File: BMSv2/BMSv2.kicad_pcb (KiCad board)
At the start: 2 copper layers, 44 x 41.2 mm, 126 parts, among them J1 Conn_01x05, J2 Conn_01x04_Socket, J3 Conn_01x02_Pin, J4 Conn_01x02_Pin, J5 Conn_01x03_Pin, Q1 AO3401A, Q10 MMBT3904, Q11 MMBT3904, Q12 MMBT3904, Q13 MMBT3904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

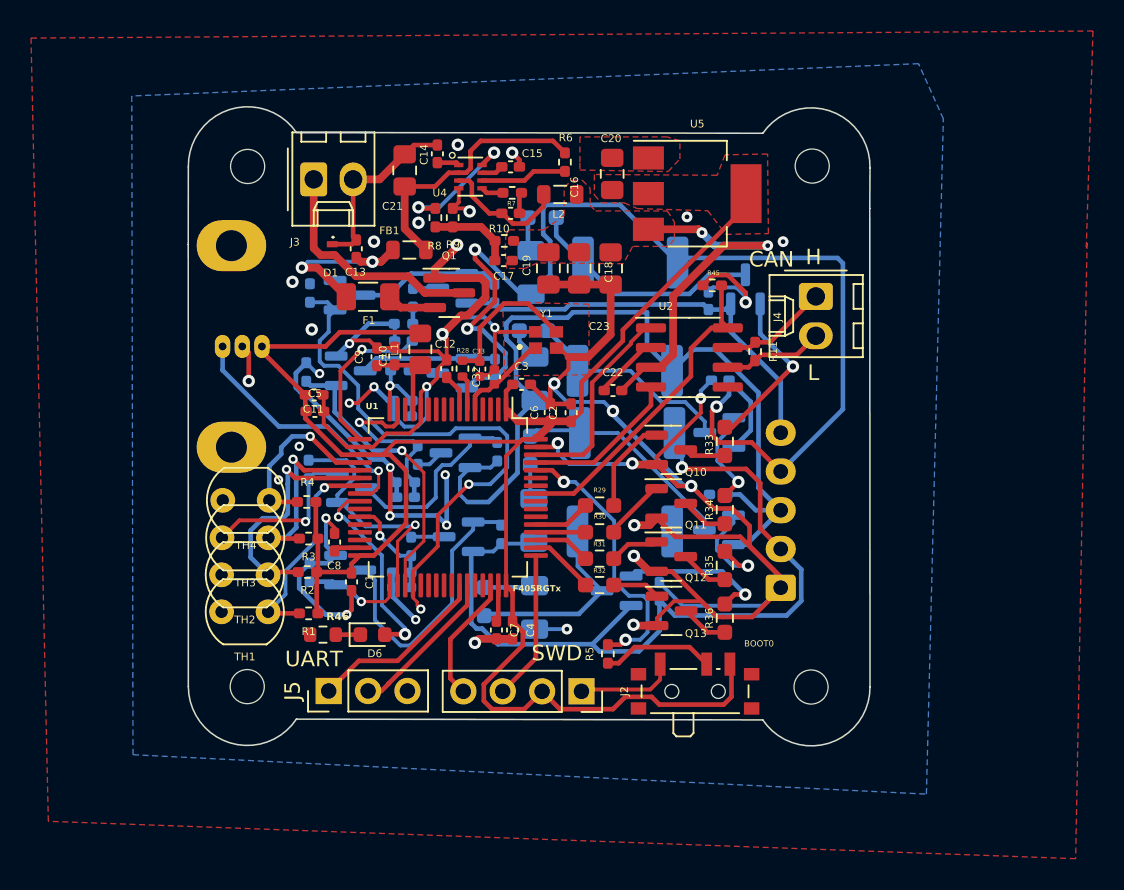
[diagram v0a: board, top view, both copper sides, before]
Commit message: silkscreen improvment
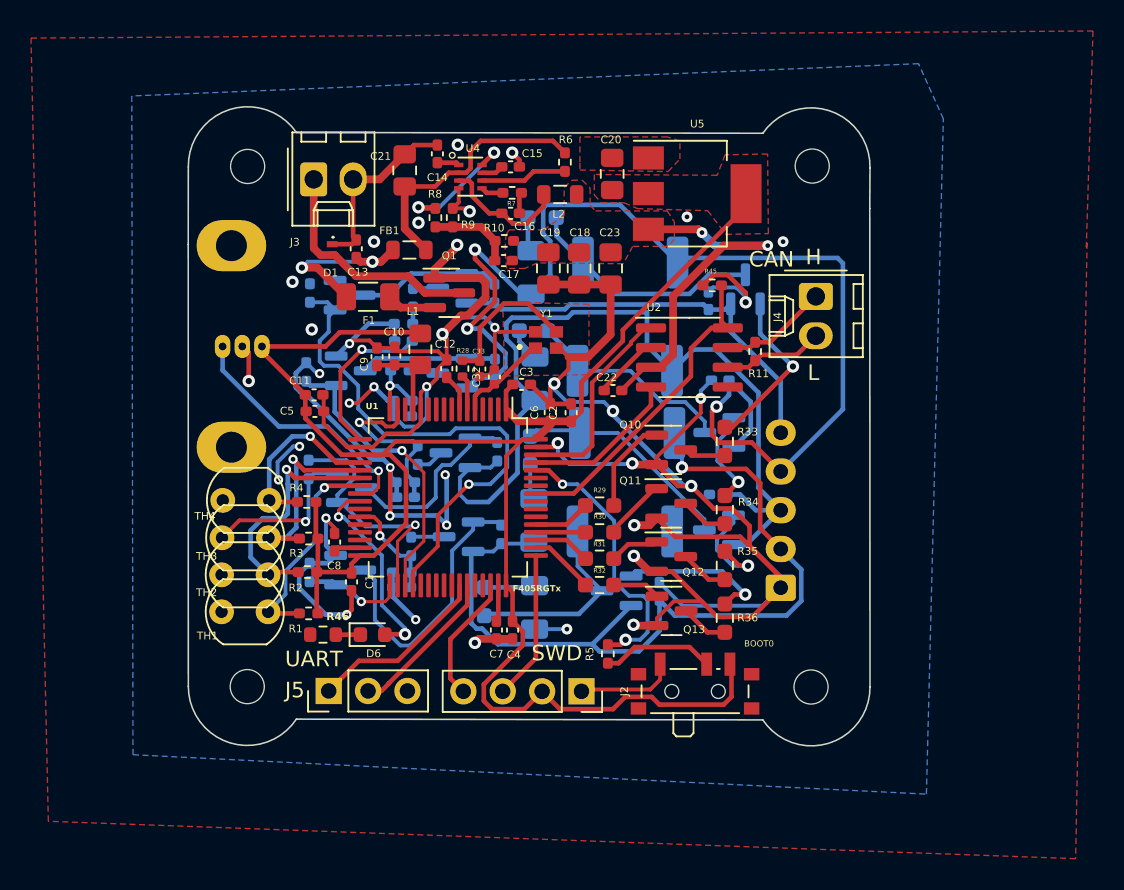
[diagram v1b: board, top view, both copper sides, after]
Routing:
- net GND: track 246.4 -> 249.5 mm
- net CELL4_M_TRIG: track 35.6 -> 33.8 mm, vias 2 -> 1

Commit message: added PGR slikscreen and export gerber files
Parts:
- added G***: LOGO, footprints:PGR_prawidlowe, B.Cu at (105.3, 49.5)
- J1: footprint Connector_JST:JST_EH_S5B-EH_1x05_P2.50mm_Horizontal -> Connector_JST:JST_XH_S5B-XH-A_1x05_P2.50mm_Horizontal; moved to F.Cu
- J3: footprint Connector_Molex:Molex_KK-254_AE-6410-02A_1x02_P2.54mm_Vertical -> Connector_Molex:Molex_PicoBlade_53048-0210_1x02_P1.25mm_Horizontal
- J4: footprint Connector_Molex:Molex_KK-254_AE-6410-02A_1x02_P2.54mm_Vertical -> Connector_Molex:Molex_PicoBlade_53261-0271_1x02-1MP_P1.25mm_Horizontal
- R12, R14, R15, R17, R18, R20, R21, R22, R23, R35: value R -> 1k
- R13: value R -> 4300
- R16: value R -> 3k
- R19, R33: value R -> 2k
- R29, R30, R31, R32: value R -> 620
- R34: value R -> 1.5k
- R36: value R -> 500
- R37: value TC -> 120
- R38, R39, R40: value R -> 120
- R41, R42, R43, R44: value R -> 30
- moved J3 2.21 mm to (79.1, 49.8), turned to 180 degrees
- moved J4 1.89 mm to (110.6, 57.5), turned to 90 degrees
- moved J1 0.87 mm to (107.9, 75.4)
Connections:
- J3 pad 1: +12V -> GND
- J3 pad 2: GND -> +12V
- J4 pad 1: CAN1+ -> CAN1-
- J4 pad 2: CAN1- -> CAN1+
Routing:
- net CELL1: track 53.3 -> 56.6 mm
- net CAN1+: track 7.05 -> 4.83 mm
- net +12V: track 15.3 -> 13.6 mm
- net CAN1-: track 6.53 -> 4.83 mm
- net Net-(Q14-B): track 10.9 -> 12.5 mm
- net CELL3: track 74.5 -> 75.9 mm
- net CELL4: track 27.2 -> 27.9 mm
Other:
- board text added: "Mieszko Celiński BMSv2"
